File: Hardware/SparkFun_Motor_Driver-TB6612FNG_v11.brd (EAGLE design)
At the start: 20.3 x 20.3 mm, 14 parts, among them U1 TB6612FNG

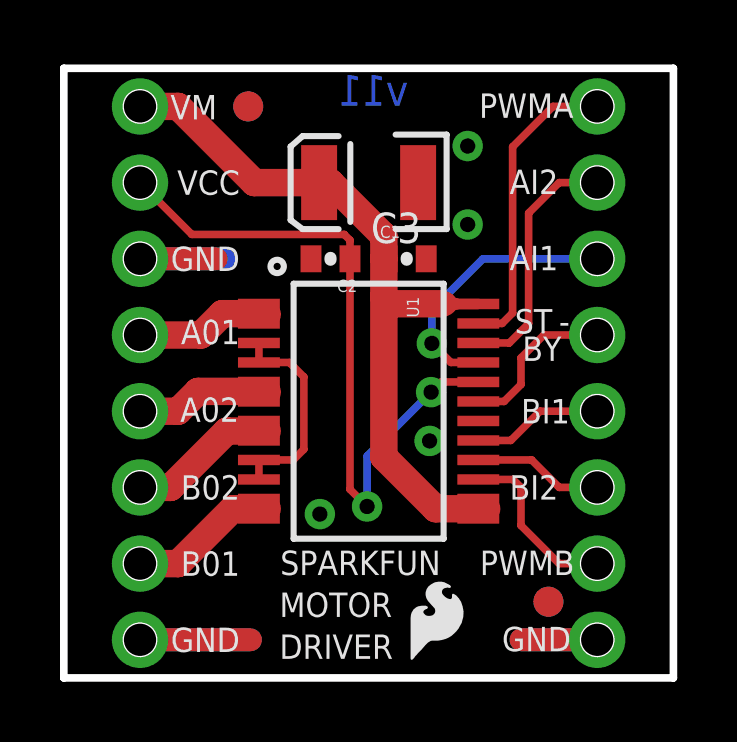
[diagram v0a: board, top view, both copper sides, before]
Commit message: Changes to design and added 1X08 conn lbr
-moved and added/removed silk
-moved fiducials and re routed some traces
-added new 1X08 offset connector lbr to repo
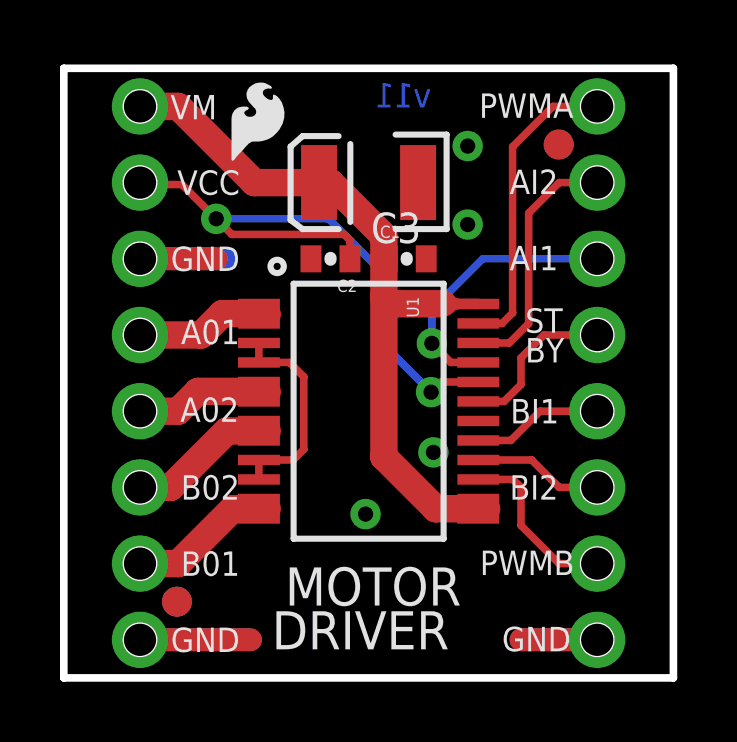
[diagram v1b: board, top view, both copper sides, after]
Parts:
- removed LOGO3: SFE_LOGO_FLAME.1_INCH, SparkFun-Aesthetics:SFE_LOGO_FLAME_.1
- added LOGO4: SFE_LOGO_NAME_FLAME.1_INCH, SparkFun-Aesthetics:SFE_LOGO_NAME_FLAME_.1
- moved LOGO1 17.7 mm to (5.31, 16.9)
- moved JP5 12.4 mm to (3.77, 2.54)
- moved JP8 12.4 mm to (3.77, 2.54)
- moved JP6 10.4 mm to (16.5, 17.8)
- moved JP7 10.4 mm to (16.5, 17.8)
- moved LOGO2 0.45 mm to (11.4, 1.71)
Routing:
- net VCC: track 23.3 -> 21.1 mm
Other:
- board text added: "MOTOR DRIVER"
- board text removed: "-"
- board text removed: "MOTOR DRVIER"
- board text removed: "SPARKFUN"
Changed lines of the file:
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@@
 <setting verticaltext="up"/>
 </settings>
-<grid distance="0.05" unitdist="inch" unit="inch" style="lines" multiple="1" display="yes" altdistance="0.001" altunitdist="inch" altunit="inch"/>
+<grid distance="0.05" unitdist="inch" unit="inch" style="lines" multiple="1" display="yes" altdistance="0.0005" altunitdist="inch" altunit="inch"/>
 <layers>
 <layer number="1" name="Top" color="4" fill="1" visible="yes" active="yes"/>
@@
 <text x="16.51" y="16.002" size="1.016" layer="22" font="vector" ratio="15" rot="MR0">AIN2</text>
 <text x="16.51" y="18.542" size="1.016" layer="22" font="vector" ratio="15" rot="MR0">PWMA</text>
-<text x="11.4808" y="19.0754" size="1.016" layer="16" font="vector" ratio="15" rot="MR0">v11</text>
+<text x="12.2428" y="19.0119" size="0.8128" layer="16" font="vector" ratio="15" rot="MR0">v11</text>
 <text x="5.1054" y="19.431" size="0.8128" layer="21" font="vector" ratio="15" rot="R180">VM</text>
 <text x="5.8674" y="16.9164" size="0.8128" layer="21" font="vector" ratio="15" rot="R180">VCC</text>
@@
 <text x="13.8684" y="3.429" size="0.8128" layer="21" font="vector" ratio="15">PWMB</text>
 <text x="14.859" y="5.9436" size="0.8128" layer="21" font="vector" ratio="15">BI2</text>
-<text x="16.8656" y="9.2964" size="0.8128" layer="21" font="vector" ratio="15" rot="R180">BI1</text>
-<text x="16.2814" y="12.2936" size="0.8128" layer="21" font="vector" ratio="15" rot="R180">ST</text>
+<text x="14.8844" y="8.4836" size="0.8128" layer="21" font="vector" ratio="15" rot="SR0">BI1</text>
+<text x="15.3797" y="11.5062" size="0.8128" layer="21" font="vector" ratio="15" rot="SR0">ST</text>
 <text x="14.859" y="13.589" size="0.8128" layer="21" font="vector" ratio="15">AI1</text>
 <text x="14.859" y="16.129" size="0.8128" layer="21" font="vector" ratio="15">AI2</text>
 <text x="13.843" y="18.669" size="0.8128" layer="21" font="vector" ratio="15">PWMA</text>
-<text x="16.5862" y="11.3792" size="0.8128" layer="21" font="vector" ratio="15" rot="R180">BY</text>
-<text x="16.8656" y="12.2936" size="0.8128" layer="21" font="vector" ratio="15" rot="R180">-</text>
-<text x="7.2136" y="3.429" size="0.8128" layer="21" font="vector" ratio="15">SPARKFUN</text>
-<text x="7.1882" y="2.032" size="0.8128" layer="21" font="vector" ratio="15">MOTOR</text>
-<text x="7.1882" y="0.635" size="0.8128" layer="21" font="vector" ratio="15">DRIVER</text>
+<text x="15.3797" y="10.5156" size="0.8128" layer="21" font="vector" ratio="15" rot="SR0">BY</text>
+<text x="7.3787" y="2.413" size="1.27" layer="21" font="vector" ratio="15">MOTOR</text>
+<text x="6.9342" y="0.9525" size="1.27" layer="21" font="vector" ratio="15">DRIVER</text>
 <text x="12.7" y="-12.7" size="1.778" layer="51" font="vector" ratio="15">Peter Dokter</text>
-<text x="10.16" y="6.1722" size="1.524" layer="22" font="vector" ratio="15" rot="MR90">TB6612FNG</text>
-<text x="8.6614" y="6.9342" size="1.016" layer="22" font="vector" ratio="15" rot="MR90">MOTOR DRVIER</text>
+<text x="8.9535" y="19.8628" size="0.889" layer="22" font="vector" ratio="15" rot="SMR270">TB6612FNG</text>
+<text x="8.9535" y="9.8425" size="0.889" layer="22" font="vector" ratio="15" rot="SMR270">MOTOR DRIVER</text>
 </plain>
 <attributes>
@@
 <attribute name="VALUE" x="13.97" y="20.32" size="1.27" layer="27" rot="R270"/>
 </element>
-<element name="JP5" library="SparkFun" package="FIDUCIAL-1X2" value="FIDUCIAL1X2" x="16.1544" y="2.54"/>
-<element name="JP6" library="SparkFun" package="FIDUCIAL-1X2" value="FIDUCIAL1X2" x="6.1468" y="19.05"/>
-<element name="JP7" library="SparkFun" package="FIDUCIAL-1X2" value="FIDUCIAL1X2" x="6.1468" y="19.05" rot="MR0"/>
-<element name="JP8" library="SparkFun" package="FIDUCIAL-1X2" value="FIDUCIAL1X2" x="16.1544" y="2.54" rot="MR0"/>
+<element name="JP5" library="SparkFun" package="FIDUCIAL-1X2" value="FIDUCIAL1X2" x="3.7719" y="2.54"/>
+<element name="JP6" library="SparkFun" package="FIDUCIAL-1X2" value="FIDUCIAL1X2" x="16.4973" y="17.78"/>
+<element name="JP7" library="SparkFun" package="FIDUCIAL-1X2" value="FIDUCIAL1X2" x="16.4973" y="17.78" rot="MR0"/>
+<element name="JP8" library="SparkFun" package="FIDUCIAL-1X2" value="FIDUCIAL1X2" x="3.7719" y="2.54" rot="MR0"/>
 <element name="FRAME1" library="SparkFun-Aesthetics" package="CREATIVE_COMMONS" value="FRAME-LETTER" x="-19.05" y="-12.7"/>
-<element name="LOGO3" library="SparkFun-Aesthetics" package="SFE_LOGO_FLAME_.1" value="SFE_LOGO_FLAME.1_INCH" x="9.2964" y="0.6096" rot="MR0"/>
-<element name="LOGO1" library="SparkFun-Aesthetics" package="SFE_LOGO_FLAME_.1" value="SFE_LOGO_FLAME.1_INCH" x="11.2776" y="0.2794"/>
-<element name="LOGO2" library="SparkFun-Aesthetics" package="OSHW-LOGO-S" value="OSHW-LOGOS" x="11.43" y="2.159" rot="MR0"/>
+<element name="LOGO1" library="SparkFun-Aesthetics" package="SFE_LOGO_FLAME_.1" value="SFE_LOGO_FLAME.1_INCH" x="5.3086" y="16.9164"/>
+<element name="LOGO2" library="SparkFun-Aesthetics" package="OSHW-LOGO-S" value="OSHW-LOGOS" x="11.3665" y="1.7145" rot="MR0"/>
+<element name="LOGO4" library="SparkFun-Aesthetics" package="SFE_LOGO_NAME_FLAME_.1" value="SFE_LOGO_NAME_FLAME.1_INCH" x="12.6365" y="18.923" rot="MR270"/>
 </elements>
 <signals>
@@
 <wire x1="7.519" y1="10.515" x2="6.504" y2="10.515" width="0.254" layer="1"/>
 <wire x1="8.001" y1="10.033" x2="7.519" y2="10.515" width="0.254" layer="1"/>
-<via x="12.192" y="7.8994" extent="1-16" drill="0.508"/>
+<via x="12.319" y="7.5184" extent="1-16" drill="0.508"/>
 <via x="13.462" y="15.113" extent="1-16" drill="0.508"/>
-<via x="8.5344" y="5.461" extent="1-16" drill="0.508"/>
+<via x="10.0584" y="5.461" extent="1-16" drill="0.508"/>
 <polygon width="0.254" layer="1" isolate="0.3048">
 <vertex x="0" y="0"/>
@@
 <wire x1="9.54" y1="13.97" x2="9.54" y2="14.59" width="0.254" layer="1"/>
 <wire x1="9.3472" y1="14.7828" x2="9.54" y2="14.59" width="0.254" layer="1"/>
-<wire x1="9.3472" y1="14.7828" x2="4.2672" y2="14.7828" width="0.254" layer="1"/>
-<wire x1="4.2672" y1="14.7828" x2="2.54" y2="16.51" width="0.254" layer="1"/>
-<wire x1="9.54" y1="13.97" x2="9.54" y2="6.2842" width="0.254" layer="1"/>
 <wire x1="13.816" y1="9.865" x2="12.5828" y2="9.865" width="0.254" layer="1"/>
 <wire x1="12.5828" y1="9.865" x2="12.2428" y2="9.525" width="0.254" layer="1"/>
 <via x="12.2428" y="9.525" extent="1-16" drill="0.508"/>
-<wire x1="9.54" y1="6.2842" x2="10.1092" y2="5.715" width="0.254" layer="1"/>
-<via x="10.1092" y="5.715" extent="1-16" drill="0.508"/>
-<wire x1="10.1092" y1="5.715" x2="10.1092" y2="7.3914" width="0.254" layer="16"/>
-<wire x1="10.1092" y1="7.3914" x2="12.2428" y2="9.525" width="0.254" layer="16"/>
+<wire x1="9.3472" y1="14.7828" x2="5.6007" y2="14.7828" width="0.254" layer="1"/>
+<wire x1="5.6007" y1="14.7828" x2="5.08" y2="15.3035" width="0.254" layer="1"/>
+<via x="5.08" y="15.3035" extent="1-16" drill="0.508"/>
+<wire x1="5.08" y1="15.3035" x2="8.8265" y2="15.3035" width="0.254" layer="16"/>
+<wire x1="8.8265" y1="15.3035" x2="10.9855" y2="13.1445" width="0.254" layer="16"/>
+<wire x1="10.9855" y1="13.1445" x2="10.9855" y2="10.7823" width="0.254" layer="16"/>
+<wire x1="10.9855" y1="10.7823" x2="12.2428" y2="9.525" width="0.254" layer="16"/>
+<wire x1="5.08" y1="15.3035" x2="3.937" y2="16.4465" width="0.254" layer="1"/>
+<wire x1="3.937" y1="16.4465" x2="2.6035" y2="16.4465" width="0.254" layer="1"/>
+<wire x1="2.6035" y1="16.4465" x2="2.54" y2="16.51" width="0.254" layer="1"/>
 </signal>
 <signal name="PWMA">

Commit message: Straightened some silk labels
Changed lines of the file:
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@@
 <setting verticaltext="up"/>
 </settings>
-<grid distance="0.05" unitdist="inch" unit="inch" style="lines" multiple="1" display="yes" altdistance="0.0005" altunitdist="inch" altunit="inch"/>
+<grid distance="0.05" unitdist="inch" unit="inch" style="lines" multiple="1" display="yes" altdistance="0.001" altunitdist="inch" altunit="inch"/>
 <layers>
 <layer number="1" name="Top" color="4" fill="1" visible="yes" active="yes"/>
@@
 <text x="16.51" y="18.542" size="1.016" layer="22" font="vector" ratio="15" rot="MR0">PWMA</text>
 <text x="12.2428" y="19.0119" size="0.8128" layer="16" font="vector" ratio="15" rot="MR0">v11</text>
-<text x="5.1054" y="19.431" size="0.8128" layer="21" font="vector" ratio="15" rot="R180">VM</text>
+<text x="5.1054" y="19.4564" size="0.8128" layer="21" font="vector" ratio="15" rot="R180">VM</text>
 <text x="5.8674" y="16.9164" size="0.8128" layer="21" font="vector" ratio="15" rot="R180">VCC</text>
 <text x="5.8674" y="14.3764" size="0.8128" layer="21" font="vector" ratio="15" rot="R180">GND</text>
 <text x="5.8674" y="1.6764" size="0.8128" layer="21" font="vector" ratio="15" rot="R180">GND</text>
-<text x="14.605" y="0.889" size="0.8128" layer="21" font="vector" ratio="15">GND</text>
-<text x="5.8674" y="11.938" size="0.8128" layer="21" font="vector" ratio="15" rot="R180">A01</text>
-<text x="5.842" y="9.3472" size="0.8128" layer="21" font="vector" ratio="15" rot="R180">A02</text>
+<text x="14.6304" y="0.8636" size="0.8128" layer="21" font="vector" ratio="15">GND</text>
+<text x="5.8674" y="11.8364" size="0.8128" layer="21" font="vector" ratio="15" rot="R180">A01</text>
+<text x="5.8674" y="9.2964" size="0.8128" layer="21" font="vector" ratio="15" rot="R180">A02</text>
 <text x="5.8674" y="6.7564" size="0.8128" layer="21" font="vector" ratio="15" rot="R180">B02</text>
 <text x="5.8674" y="4.2164" size="0.8128" layer="21" font="vector" ratio="15" rot="R180">B01</text>
-<text x="13.8684" y="3.429" size="0.8128" layer="21" font="vector" ratio="15">PWMB</text>
-<text x="14.859" y="5.9436" size="0.8128" layer="21" font="vector" ratio="15">BI2</text>
+<text x="13.8684" y="3.4036" size="0.8128" layer="21" font="vector" ratio="15">PWMB</text>
+<text x="14.8844" y="5.9436" size="0.8128" layer="21" font="vector" ratio="15">BI2</text>
 <text x="14.8844" y="8.4836" size="0.8128" layer="21" font="vector" ratio="15" rot="SR0">BI1</text>
 <text x="15.3797" y="11.5062" size="0.8128" layer="21" font="vector" ratio="15" rot="SR0">ST</text>
-<text x="14.859" y="13.589" size="0.8128" layer="21" font="vector" ratio="15">AI1</text>
-<text x="14.859" y="16.129" size="0.8128" layer="21" font="vector" ratio="15">AI2</text>
-<text x="13.843" y="18.669" size="0.8128" layer="21" font="vector" ratio="15">PWMA</text>
+<text x="14.8844" y="13.5636" size="0.8128" layer="21" font="vector" ratio="15">AI1</text>
+<text x="14.8844" y="16.1036" size="0.8128" layer="21" font="vector" ratio="15">AI2</text>
+<text x="13.8938" y="18.6436" size="0.8128" layer="21" font="vector" ratio="15">PWMA</text>
 <text x="15.3797" y="10.5156" size="0.8128" layer="21" font="vector" ratio="15" rot="SR0">BY</text>
 <text x="7.3787" y="2.413" size="1.27" layer="21" font="vector" ratio="15">MOTOR</text>

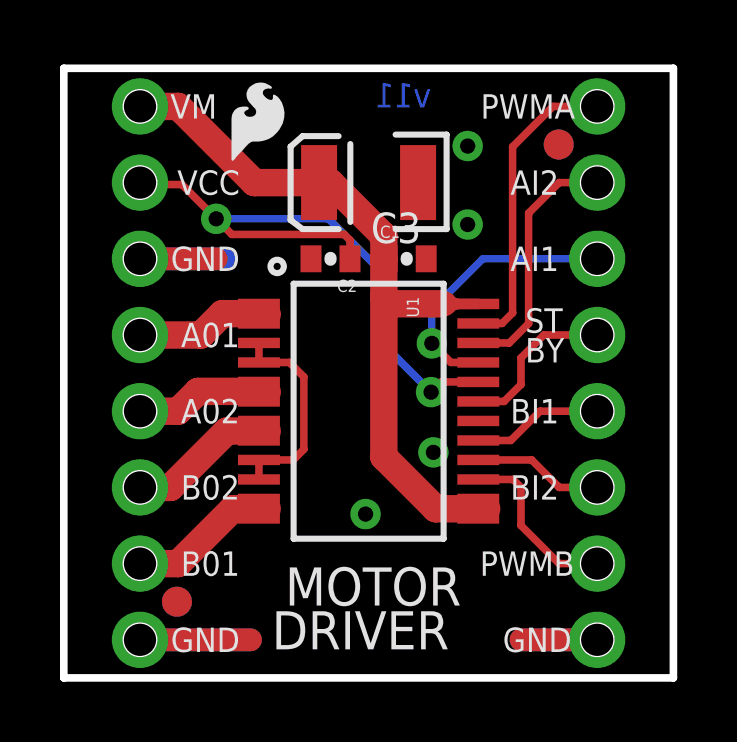
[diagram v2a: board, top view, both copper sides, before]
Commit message: Changes to SCH and BRD
-swapped to use micro-fiducials
-added revised by
-completed DRC
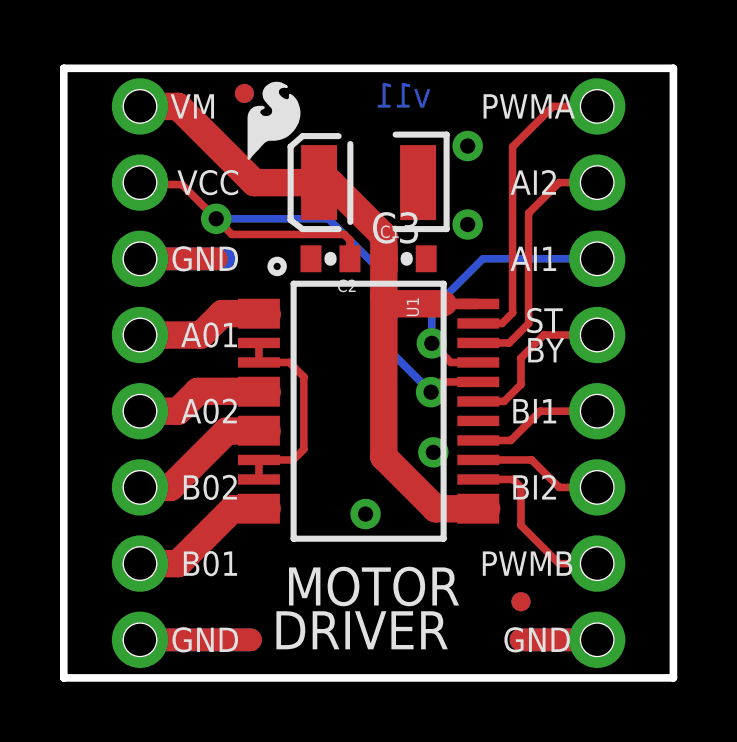
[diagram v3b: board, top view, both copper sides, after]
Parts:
- removed JP5, JP6, JP7, JP8: FIDUCIAL1X2, SparkFun:FIDUCIAL-1X2
- added FD1, FD2, FD3, FD4: FIDUCIALUFIDUCIAL, SparkFun-Aesthetics:FIDUCIAL-MICRO
- moved LOGO1 0.53 mm to (5.84, 16.9)
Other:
- board text added: "Eric Orosel"
- board text added: "Revised by:"
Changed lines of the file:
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@@
 <setting verticaltext="up"/>
 </settings>
-<grid distance="0.05" unitdist="inch" unit="inch" style="lines" multiple="1" display="yes" altdistance="0.001" altunitdist="inch" altunit="inch"/>
+<grid distance="0.05" unitdist="inch" unit="inch" style="lines" multiple="1" display="yes" altdistance="0.005" altunitdist="inch" altunit="inch"/>
 <layers>
 <layer number="1" name="Top" color="4" fill="1" visible="yes" active="yes"/>
@@
 <layer number="47" name="Measures" color="7" fill="1" visible="no" active="yes"/>
 <layer number="48" name="Document" color="7" fill="1" visible="no" active="yes"/>
-<layer number="49" name="Reference" color="13" fill="1" visible="yes" active="yes"/>
+<layer number="49" name="Reference" color="13" fill="1" visible="no" active="yes"/>
 <layer number="50" name="dxf" color="7" fill="1" visible="no" active="yes"/>
 <layer number="51" name="tDocu" color="6" fill="1" visible="yes" active="yes"/>
@@
 <text x="13.8938" y="18.6436" size="0.8128" layer="21" font="vector" ratio="15">PWMA</text>
 <text x="15.3797" y="10.5156" size="0.8128" layer="21" font="vector" ratio="15" rot="SR0">BY</text>
-<text x="7.3787" y="2.413" size="1.27" layer="21" font="vector" ratio="15">MOTOR</text>
+<text x="7.3533" y="2.413" size="1.27" layer="21" font="vector" ratio="15">MOTOR</text>
 <text x="6.9342" y="0.9525" size="1.27" layer="21" font="vector" ratio="15">DRIVER</text>
-<text x="12.7" y="-12.7" size="1.778" layer="51" font="vector" ratio="15">Peter Dokter</text>
+<text x="12.7" y="-12.7" size="1.778" layer="51" font="vector" ratio="10">Peter Dokter</text>
 <text x="8.9535" y="19.8628" size="0.889" layer="22" font="vector" ratio="15" rot="SMR270">TB6612FNG</text>
 <text x="8.9535" y="9.8425" size="0.889" layer="22" font="vector" ratio="15" rot="SMR270">MOTOR DRIVER</text>
+<text x="-7.62" y="-15.24" size="1.778" layer="51" font="vector" ratio="10">Revised by:</text>
+<text x="12.7" y="-15.24" size="1.778" layer="51" font="vector" ratio="10">Eric Orosel</text>
 </plain>
 <attributes>
@@
 <attribute name="VALUE" x="13.97" y="20.32" size="1.27" layer="27" rot="R270"/>
 </element>
-<element name="JP5" library="SparkFun" package="FIDUCIAL-1X2" value="FIDUCIAL1X2" x="3.7719" y="2.54"/>
-<element name="JP6" library="SparkFun" package="FIDUCIAL-1X2" value="FIDUCIAL1X2" x="16.4973" y="17.78"/>
-<element name="JP7" library="SparkFun" package="FIDUCIAL-1X2" value="FIDUCIAL1X2" x="16.4973" y="17.78" rot="MR0"/>
-<element name="JP8" library="SparkFun" package="FIDUCIAL-1X2" value="FIDUCIAL1X2" x="3.7719" y="2.54" rot="MR0"/>
 <element name="FRAME1" library="SparkFun-Aesthetics" package="CREATIVE_COMMONS" value="FRAME-LETTER" x="-19.05" y="-12.7"/>
-<element name="LOGO1" library="SparkFun-Aesthetics" package="SFE_LOGO_FLAME_.1" value="SFE_LOGO_FLAME.1_INCH" x="5.3086" y="16.9164"/>
+<element name="LOGO1" library="SparkFun-Aesthetics" package="SFE_LOGO_FLAME_.1" value="SFE_LOGO_FLAME.1_INCH" x="5.842" y="16.9418"/>
 <element name="LOGO2" library="SparkFun-Aesthetics" package="OSHW-LOGO-S" value="OSHW-LOGOS" x="11.3665" y="1.7145" rot="MR0"/>
 <element name="LOGO4" library="SparkFun-Aesthetics" package="SFE_LOGO_NAME_FLAME_.1" value="SFE_LOGO_NAME_FLAME.1_INCH" x="12.6365" y="18.923" rot="MR270"/>
+<element name="FD1" library="SparkFun-Aesthetics" package="FIDUCIAL-MICRO" value="FIDUCIALUFIDUCIAL" x="6.0198" y="19.4818" rot="MR0"/>
+<element name="FD2" library="SparkFun-Aesthetics" package="FIDUCIAL-MICRO" value="FIDUCIALUFIDUCIAL" x="15.24" y="2.54"/>
+<element name="FD3" library="SparkFun-Aesthetics" package="FIDUCIAL-MICRO" value="FIDUCIALUFIDUCIAL" x="15.24" y="2.54" rot="MR0"/>
+<element name="FD4" library="SparkFun-Aesthetics" package="FIDUCIAL-MICRO" value="FIDUCIALUFIDUCIAL" x="6.0198" y="19.4818"/>
 </elements>
 <signals>
@@
 <wire x1="10.668" y1="13.97" x2="10.668" y2="14.732" width="0.9144" layer="1"/>
 <wire x1="10.668" y1="13.97" x2="10.78" y2="13.97" width="0.254" layer="1"/>
-<wire x1="13.062" y1="12.465" x2="13.816" y2="12.465" width="0.3556" layer="1"/>
-<wire x1="13.062" y1="12.465" x2="13.0556" y2="12.4714" width="0.3556" layer="1"/>
 <wire x1="10.668" y1="7.366" x2="10.668" y2="12.7" width="0.9144" layer="1"/>
 <wire x1="10.668" y1="12.7" x2="10.668" y2="13.97" width="0.9144" layer="1"/>
@@
 <wire x1="13.816" y1="5.4848" x2="13.816" y2="5.315" width="0.254" layer="1"/>
 <wire x1="13.97" y1="5.6388" x2="13.816" y2="5.4848" width="0.254" layer="1"/>
-<wire x1="12.8334" y1="12.465" x2="13.062" y2="12.465" width="0.4064" layer="1"/>
-<wire x1="12.8334" y1="12.465" x2="12.954" y2="12.4714" width="0.4064" layer="1"/>
-<wire x1="12.5794" y1="12.465" x2="12.8334" y2="12.465" width="0.6096" layer="1"/>
-<wire x1="12.7" y1="12.4714" x2="12.5794" y2="12.465" width="0.6096" layer="1"/>
 <wire x1="12.573" y1="12.4714" x2="12.7" y2="12.4714" width="0.8128" layer="1"/>
 <wire x1="10.8966" y1="12.4714" x2="12.573" y2="12.4714" width="0.9144" layer="1"/>
@@
 <wire x1="6.35" y1="16.51" x2="3.81" y2="19.05" width="0.9144" layer="1"/>
 <wire x1="8.51" y1="16.51" x2="6.35" y2="16.51" width="0.9144" layer="1"/>
+<wire x1="13.816" y1="12.465" x2="12.7064" y2="12.465" width="0.34798125" layer="1"/>
+<wire x1="12.7064" y1="12.465" x2="12.7" y2="12.4714" width="0.3429" layer="1"/>
 </signal>
 <signal name="VCC">
